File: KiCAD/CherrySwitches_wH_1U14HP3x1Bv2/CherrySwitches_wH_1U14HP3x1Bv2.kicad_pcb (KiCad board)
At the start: 2 copper layers, 70.8 x 39.7 mm, 8 parts

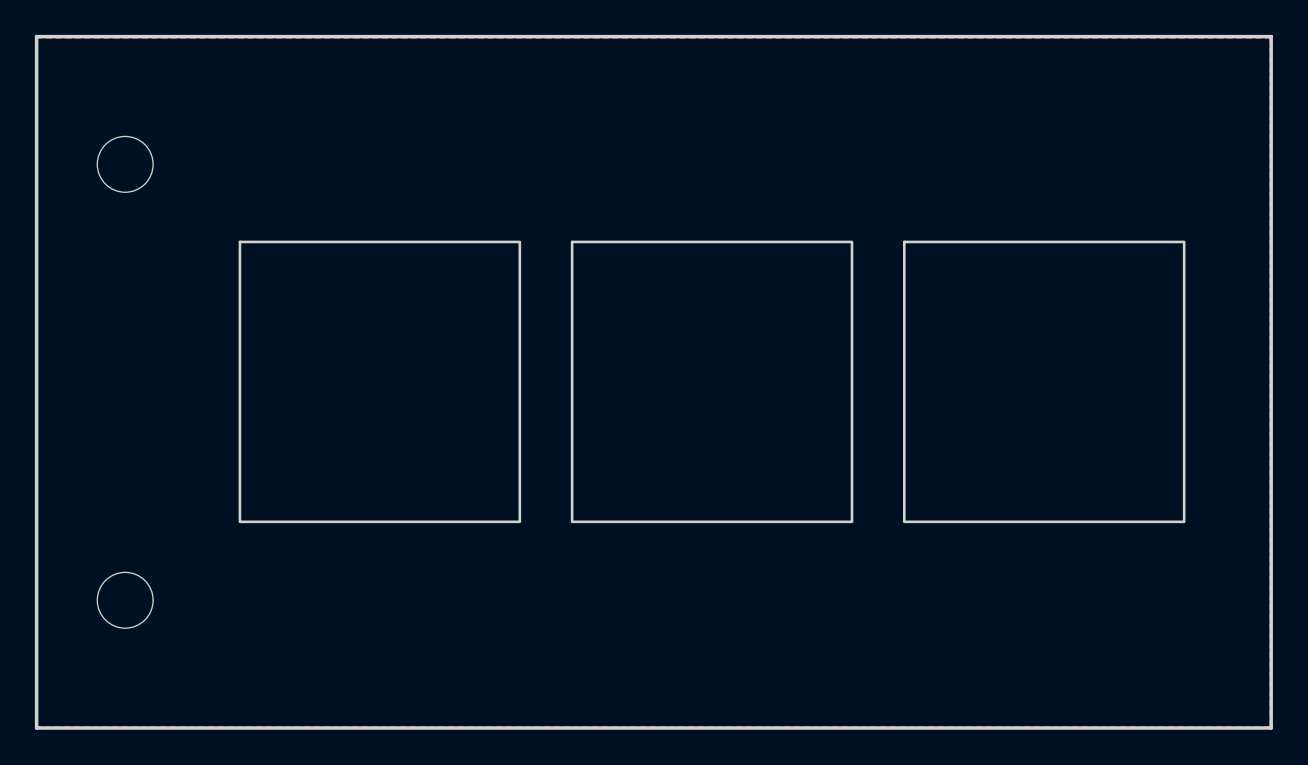
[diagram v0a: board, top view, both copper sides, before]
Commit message: updated all modules to use plated through-holes wherever possible
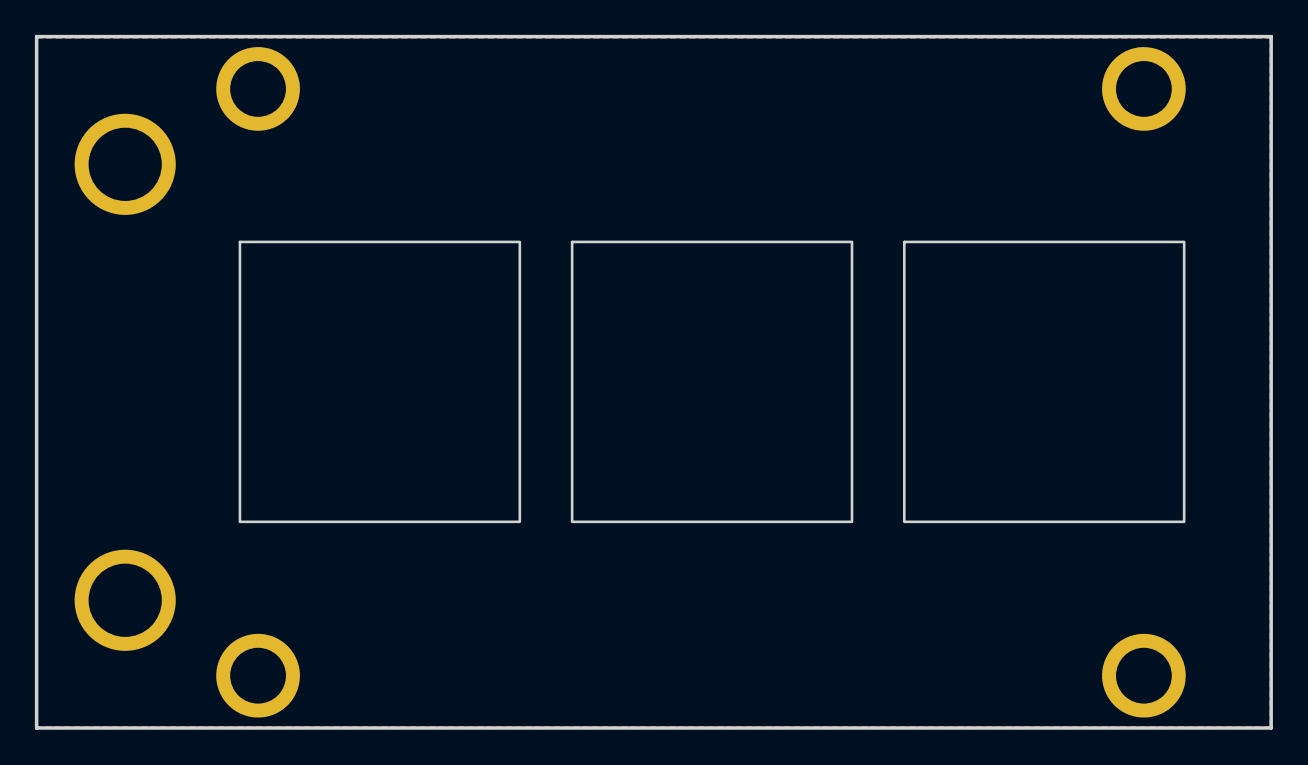
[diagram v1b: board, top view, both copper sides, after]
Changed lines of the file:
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@@
+			)
+		)
+		(property "Source" "https://www.aliexpress.com/item/1005007242440186.html"
+			(at 0 36 0)
+			(layer "F.Fab")
+			(hide yes)
+			(effects
+				(font
+					(size 1 1)
+					(thickness 0.1)
+				)
 			)
 		)
@@
 			)
 		)
-		(pad "" np_thru_hole circle
+		(pad "" thru_hole circle
 			(at 0 0)
-			(size 3.2 3.2)
-			(drill 3.2)
+			(size 5.8 5.8)
+			(drill 4.2)
 			(layers "*.Cu" "*.Mask")
-		)
-		(pad "" np_thru_hole circle
+			(remove_unused_layers no)
+		)
+		(pad "" thru_hole circle
 			(at 0 25)
-			(size 3.2 3.2)
-			(drill 3.2)
+			(size 5.8 5.8)
+			(drill 4.2)
 			(layers "*.Cu" "*.Mask")
+			(remove_unused_layers no)
 		)
 		(embedded_fonts no)
@@
 			)
 		)
-		(pad "" np_thru_hole oval
+		(pad "" thru_hole circle
 			(at 0 0)
-			(size 4.34 3.2)
-			(drill oval 4.34 3.2)
+			(size 4.8 4.8)
+			(drill 3.2)
 			(layers "*.Cu" "*.Mask")
+			(remove_unused_layers no)
 		)
 		(embedded_fonts no)
@@
 			)
 		)
-		(pad "" np_thru_hole oval
+		(pad "" thru_hole circle
 			(at 0 0)
-			(size 4.34 3.2)
-			(drill oval 4.34 3.2)
+			(size 4.8 4.8)
+			(drill 3.2)
 			(layers "*.Cu" "*.Mask")
+			(remove_unused_layers no)
 		)
 		(embedded_fonts no)
@@
 			)
 		)
-		(pad "" np_thru_hole oval
+		(pad "" thru_hole circle
 			(at 0 0)
-			(size 4.34 3.2)
-			(drill oval 4.34 3.2)
+			(size 4.8 4.8)
+			(drill 3.2)
 			(layers "*.Cu" "*.Mask")
+			(remove_unused_layers no)
 		)
 		(embedded_fonts no)
@@
 			)
 		)
-		(pad "" np_thru_hole oval
+		(pad "" thru_hole circle
 			(at 0 0)
-			(size 4.34 3.2)
-			(drill oval 4.34 3.2)
+			(size 4.8 4.8)
+			(drill 3.2)
 			(layers "*.Cu" "*.Mask")
+			(remove_unused_layers no)
 		)
 		(embedded_fonts no)
